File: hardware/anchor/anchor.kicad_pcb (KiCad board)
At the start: 2 copper layers, 50.1 x 50 mm, 94 parts, among them J2 USB_C_Receptacle_USB2.0_16P, J3 STM SWD, J4 BLE SWD, J5 BATTERY, SW1 SW_DIP_x03, SW2 RESET, SW3 BOOT, SW4 USER, U1 BQ24075RGT, U2 TPS63070RNMR, U3 USBLC6-2SC6, U4 STM32F411CEUx, U6 FSC-BT630, Y1 NX3225SA-24MHz

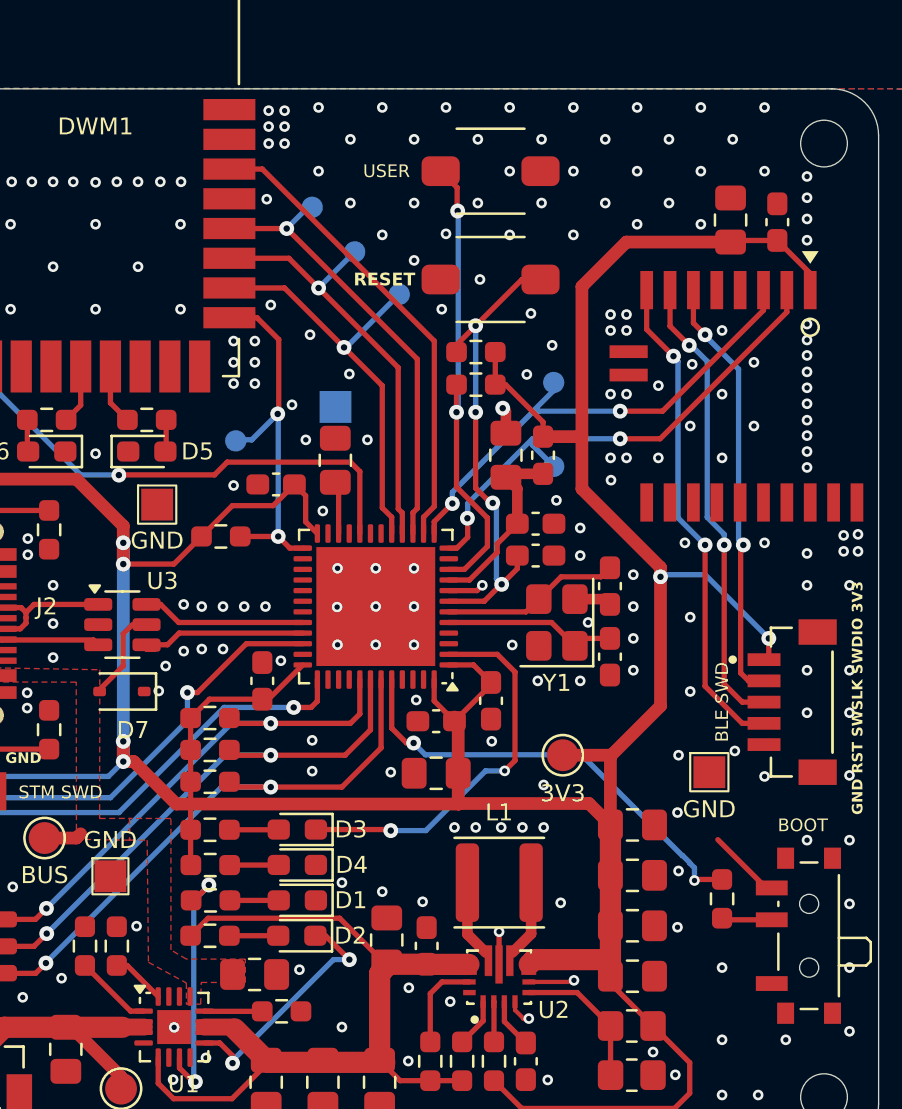
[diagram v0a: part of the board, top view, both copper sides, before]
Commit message: update(anchor): Clear DRC errors and release anchor rev 0.2
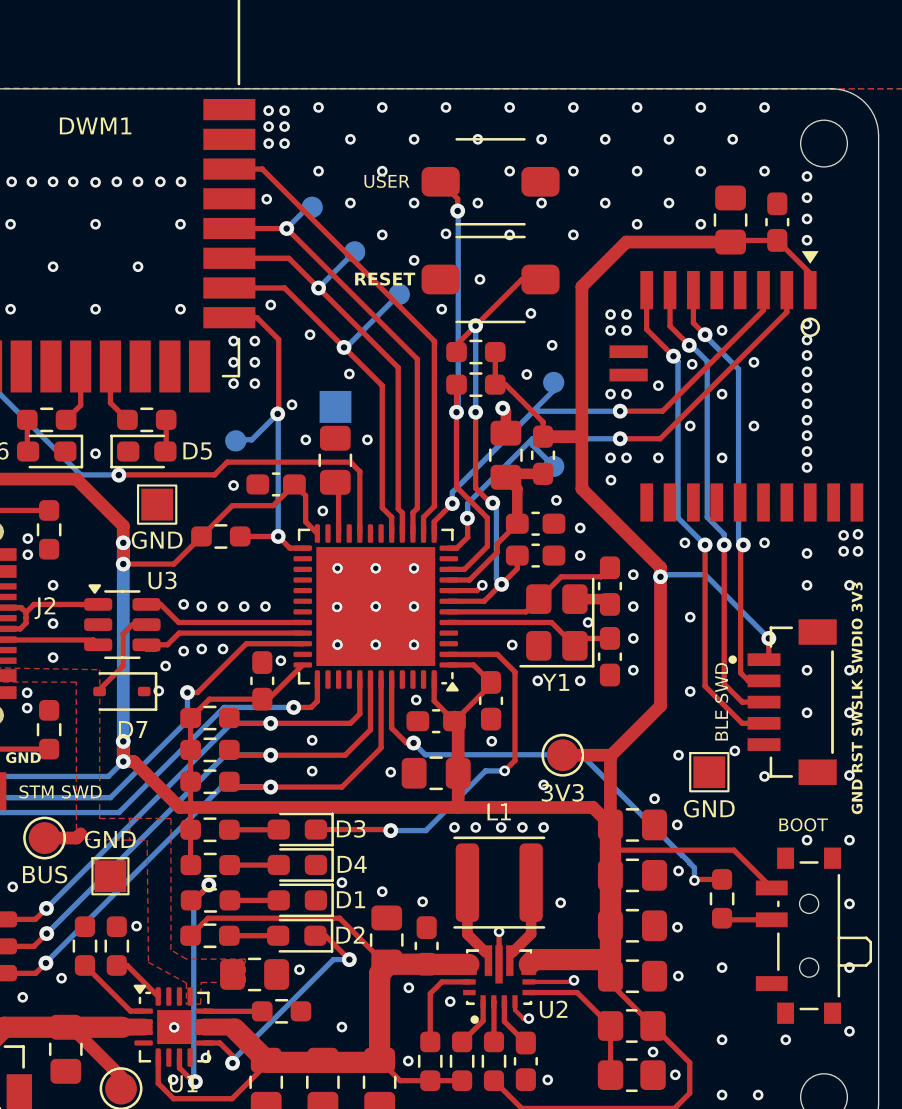
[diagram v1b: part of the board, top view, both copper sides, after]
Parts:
- moved SW4 0.50 mm to (224.1, 67.0)
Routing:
- net +3.3V: track 192.6 -> 197.8 mm
- net GND: vias 258 -> 261
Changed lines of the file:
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@@
 	(footprint "My_Tactile:SW_Tactile_SMD_3x4mm_2pin_update"
 		(layer "F.Cu")
-		(at 224.1 66.5 180)
+		(at 224.1 67 180)
 		(descr "Tactile switch SMD 2-pin, body 3x4x2 mm, pads 1.8x1.4 mm, 4.7 mm pitch")
 		(tags "tactile switch 3x4 2pin SMD")
@@
 	)
 	(via
+		(at 231.82 96.05)
+		(size 0.5)
+		(drill 0.25)
+		(layers "F.Cu" "B.Cu")
+		(free yes)
+		(net 1)
+	)
+	(via
 		(at 197.8 103)
 		(size 0.5)
@@
 	)
 	(via
-		(at 232.9 96.7)
+		(at 232.89 97.28)
 		(size 0.5)
 		(drill 0.25)
@@
 	)
 	(via
+		(at 219 66.5)
+		(size 0.5)
+		(drill 0.25)
+		(layers "F.Cu" "B.Cu")
+		(free yes)
+		(net 1)
+	)
+	(via
 		(at 233.5 91)
 		(size 0.5)
@@
 	)
 	(via
+		(at 232.94 104.4)
+		(size 0.5)
+		(drill 0.25)
+		(layers "F.Cu" "B.Cu")
+		(free yes)
+		(net 1)
+	)
+	(via
 		(at 223.5 65)
 		(size 0.5)
@@
 	)
 	(segment
+		(start 222.575 96.455)
+		(end 222.58 96.46)
+		(width 0.6)
+		(layer "F.Cu")
+		(net 5)
+	)
+	(segment
 		(start 210.8625 91.3625)
 		(end 213.35 91.3625)
@@
 	)
 	(segment
+		(start 209.975 96.46)
+		(end 209.975 96.325)
+		(width 0.25)
+		(layer "F.Cu")
+		(net 5)
+	)
+	(segment
 		(start 228.4 71.9296)
 		(end 230.4921 69.8375)
@@
 	)
 	(segment
+		(start 229.7425 97.283)
+		(end 228.9195 96.46)
+		(width 0.6)
+		(layer "F.Cu")
+		(net 5)
+	)
+	(segment
 		(start 209.975 92.25)
 		(end 209.975 91.94525)
@@
 	)
 	(segment
-		(start 222.625 96.275)
-		(end 222.6 96.3)
-		(width 0.6)
-		(layer "F.Cu")
-		(net 5)
-	)
-	(segment
-		(start 209.3 96.3)
-		(end 209.95 96.3)
-		(width 0.6)
-		(layer "F.Cu")
-		(net 5)
-	)
-	(segment
 		(start 199.4 81)
 		(end 198.7 81)
@@
 	)
 	(segment
+		(start 207.3 94.3)
+		(end 209.46 96.46)
+		(width 0.6)
+		(layer "F.Cu")
+		(net 5)
+	)
+	(segment
 		(start 229.7425 103.625)
 		(end 229.7425 104.40575)
@@
 	)
 	(segment
-		(start 209.975 96.275)
-		(end 209.95 96.3)
-		(width 0.25)
-		(layer "F.Cu")
-		(net 5)
-	)
-	(segment
 		(start 232.1 85.6)
 		(end 232.1 85.16)
@@
 	(segment
 		(start 229.7425 99.65725)
-		(end 229.7425 97.283)
+		(end 229.7425 98.41)
 		(width 1)
 		(layer "F.Cu")
@@
 	)
 	(segment
-		(start 222.575 96.275)
-		(end 222.6 96.3)
-		(width 0.6)
-		(layer "F.Cu")
-		(net 5)
-	)
-	(segment
 		(start 209.975 97.51)
 		(end 209.975 98.9875)
@@
 	)
 	(segment
-		(start 237.075 100.25)
-		(end 234.8 97.975)
-		(width 0.25)
+		(start 222.58 96.46)
+		(end 209.975 96.46)
+		(width 0.6)
 		(layer "F.Cu")
 		(net 5)
@@
 	)
 	(segment
-		(start 207.3 94.3)
-		(end 209.3 96.3)
+		(start 222.575 94.85)
+		(end 222.575 96.455)
 		(width 0.6)
 		(layer "F.Cu")
@@
 	)
 	(segment
-		(start 209.975 96.325)
-		(end 209.95 96.3)
+		(start 229.7425 98.41)
+		(end 229.8025 98.47)
 		(width 0.25)
 		(layer "F.Cu")
@@
 	)
 	(segment
+		(start 228.9195 96.46)
+		(end 222.58 96.46)
+		(width 0.6)
+		(layer "F.Cu")
+		(net 5)
+	)
+	(segment
 		(start 224.3 90.575)
 		(end 224.275 90.575)
@@
 	)
 	(segment
-		(start 228.7345 96.275)
-		(end 229.7425 97.283)
-		(width 0.6)
-		(layer "F.Cu")
-		(net 5)
-	)
-	(segment
 		(start 233.476 108.476)
 		(end 231.75 106.75)
@@
 	)
 	(segment
-		(start 222.6 96.3)
-		(end 209.95 96.3)
-		(width 0.6)
-		(layer "F.Cu")
-		(net 5)
-	)
-	(segment
 		(start 224.32125 76.55)
 		(end 224.32125 75.017005)
@@
 	(segment
 		(start 209.975 97.51)
-		(end 209.975 96.325)
+		(end 209.975 96.46)
 		(width 0.25)
 		(layer "F.Cu")
@@
 	)
 	(segment
-		(start 222.625 96.275)
-		(end 228.7345 96.275)
-		(width 0.6)
-		(layer "F.Cu")
-		(net 5)
-	)
-	(segment
 		(start 197.75 81)
 		(end 197.5 81)
@@
 	)
 	(segment
+		(start 229.8025 98.47)
+		(end 235.56 98.47)
+		(width 0.25)
+		(layer "F.Cu")
+		(net 5)
+	)
+	(segment
 		(start 222.575 92.575)
 		(end 222.4 92.4)
@@
 	)
 	(segment
+		(start 229.7425 98.41)
+		(end 229.7425 97.283)
+		(width 1)
+		(layer "F.Cu")
+		(net 5)
+	)
+	(segment
 		(start 206.80475 83.20475)
 		(end 204.6 81)
@@
 	)
 	(segment
+		(start 235.56 98.47)
+		(end 237.34 100.25)
+		(width 0.25)
+		(layer "F.Cu")
+		(net 5)
+	)
+	(segment
 		(start 237.6 69.7625)
 		(end 235.475 69.7625)
@@
 	)
 	(segment
-		(start 222.575 94.85)
-		(end 222.575 96.275)
+		(start 209.46 96.46)
+		(end 209.975 96.46)
 		(width 0.6)
 		(layer "F.Cu")
@@
 	)
 	(segment
-		(start 222.525 68.35)
-		(end 222.525 67.275)
+		(start 222.55 68.375)
+		(end 222.55 67.8)
 		(width 0.25)
 		(layer "F.Cu")
@@
 	)
 	(segment
-		(start 222.525 67.275)
-		(end 221.75 66.5)
-		(width 0.25)
-		(layer "F.Cu")
-		(net 31)
-	)
-	(segment
 		(start 222.49625 77.85)
 		(end 222.49625 76.55)
@@
 		(width 0.25)
 		(layer "F.Cu")
+		(net 31)
+	)
+	(segment
+		(start 222.55 67.8)
+		(end 221.75 67)
+		(width 0.25)
+		(layer "F.Cu")

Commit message: update(hw): Apply design changes to anchor
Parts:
- removed C3: 10u, Capacitor_SMD:C_0805_2012Metric_Pad1.18x1.45mm_HandSolder
- removed the D1 at (215.0, 100.8)
- removed the R14 at (224.3, 108.4)
- removed the R3 at (210.9, 99.2)
- removed the R5 at (206.5, 103.0)
- removed the SW3 at (238.8, 102.5)
- removed TP15: BATT, TestPoint:TestPoint_Pad_D1.5mm
- added C13: 22u, Capacitor_SMD:C_0805_2012Metric_Pad1.18x1.45mm_HandSolder, F.Cu at (235.4, 100.9)
- added C24: DNP, Capacitor_SMD:C_01005_0402Metric, F.Cu at (241.1, 85.5)
- added C26: DNP, Capacitor_SMD:C_01005_0402Metric, F.Cu at (241.1, 88.0)
- added D5: RED, LED_SMD:LED_0603_1608Metric_Pad1.05x0.95mm_HandSolder, F.Cu at (215.9, 100.3)
- added J3: BLE_Conn, Connector_Coaxial:U.FL_Hirose_U.FL-R-SMT-1_Vertical, F.Cu at (238.2, 88.8)
- added L2: DNP, Inductor_SMD:L_0402_1005Metric, F.Cu at (241.4, 86.8)
- added Q1: AO664, Package_SO:TSOP-6_1.65x3.05mm_P0.95mm, F.Cu at (219.3, 106.1)
- added R18: 10K, Resistor_SMD:R_0603_1608Metric_Pad0.98x0.95mm_HandSolder, F.Cu at (219.8, 94.6)
- added R22: 2.2k, Resistor_SMD:R_0603_1608Metric_Pad0.98x0.95mm_HandSolder, F.Cu at (212.0, 97.3)
- added R23: 2.2k, Resistor_SMD:R_0603_1608Metric_Pad0.98x0.95mm_HandSolder, F.Cu at (212.0, 100.3)
- added R6: 3.56k, Resistor_SMD:R_0603_1608Metric_Pad0.98x0.95mm_HandSolder, F.Cu at (212.0, 103.0)
- added R7: 10k, Resistor_SMD:R_0603_1608Metric_Pad0.98x0.95mm_HandSolder, F.Cu at (209.7, 103.9)
- added R8: 470k, Resistor_SMD:R_0805_2012Metric_Pad1.20x1.40mm_HandSolder, F.Cu at (235.4, 108.1)
- added SW1: PWR, Button_Switch_SMD:SW_Push_1P1T-MP_NO_Horizontal_Alps_SKRTLAE010, F.Cu at (217.6, 111.0)
- added TP11: BATT, TestPoint:TestPoint_Pad_D1.5mm, F.Cu at (205.7, 108.9)
- added TP16: SYS, TestPoint:TestPoint_Pad_D1.5mm, F.Cu at (220.2, 101.0)
- added U4: BQ24075RGT, Package_DFN_QFN:VQFN-16-1EP_3x3mm_P0.5mm_EP1.6x1.6mm, F.Cu at (213.9, 106.1)
- C10, C11: value 22u -> 10u
- C12: value DNP -> 22u
- C5: value 1u -> 100n; footprint Capacitor_SMD:C_0805_2012Metric_Pad1.18x1.45mm_HandSolder -> Capacitor_SMD:C_0603_1608Metric_Pad1.08x0.95mm_HandSolder
- C6: value 4.7u -> 100n; footprint Capacitor_SMD:C_0805_2012Metric_Pad1.18x1.45mm_HandSolder -> Capacitor_SMD:C_0603_1608Metric_Pad1.08x0.95mm_HandSolder
- C7: value 4.7u -> 1u
- C8: value 100n -> 1u
- C9: value 10u -> 4.7u
- D2: value YELLOW -> GREEN
- R10: value 6k -> 10k
- R11: value 6k -> 100k
- R12: value 470k -> 10k; footprint Resistor_SMD:R_0805_2012Metric_Pad1.20x1.40mm_HandSolder -> Resistor_SMD:R_0603_1608Metric_Pad0.98x0.95mm_HandSolder
- R13: value 150k -> 10k; footprint Resistor_SMD:R_0805_2012Metric_Pad1.20x1.40mm_HandSolder -> Resistor_SMD:R_0603_1608Metric_Pad0.98x0.95mm_HandSolder
- R19: value 10K -> 2.2k
- R2: value 3.1k -> 10k
- R4: value 10k -> 3.1k
- R9: value 10k -> 150k; footprint Resistor_SMD:R_0603_1608Metric_Pad0.98x0.95mm_HandSolder -> Resistor_SMD:R_0805_2012Metric_Pad1.20x1.40mm_HandSolder
- TP3: footprint TestPoint:TestPoint_Pad_D1.5mm -> TestPoint:TestPoint_Pad_D1.0mm
- U1: value BQ24075RGT -> MAX17048G_T10; footprint Package_DFN_QFN:VQFN-16-1EP_3x3mm_P0.5mm_EP1.6x1.6mm -> Package_SON:SON-8-1EP_3x2mm_P0.5mm_EP1.4x1.6mm
- U5: renamed from U6; footprint Other_Footprint:FSC-BT630 -> other_footprint:FSC-BT630
- moved R9 31.3 mm to (235.4, 110.4), turned to 0 degrees
- moved C6 28.5 mm to (232.5, 110.1)
- moved J5 27.3 mm to (232.8, 64.9), turned to 0 degrees
- moved D2 24.4 mm to (233.7, 86.9), turned to 90 degrees
- moved R10 21.5 mm to (230.9, 110.1), turned to -90 degrees
- moved C9 20.8 mm to (210.6, 109.2), turned to -90 degrees
- moved R2 14.1 mm to (227.7, 110.1), turned to -90 degrees
- moved R19 13.9 mm to (235.2, 86.9)
- moved R11 12.3 mm to (222.6, 104.7), turned to 90 degrees
- moved C11 11.5 mm to (219.3, 103.3)
- moved C2 9.42 mm to (225.6, 108.6)
- moved R13 8.89 mm to (221.9, 108.4), turned to 90 degrees
- moved R12 8.47 mm to (223.6, 102.2)
- moved R4 8.08 mm to (223.6, 100.7), turned to 0 degrees
- moved TP4 7.97 mm to (239.4, 101.0)
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- renumbered C23 to C15, C13 to C16, C22 to C17, C14 to C18, C15 to C19, C16 to C20, C17 to C21, C18 to C22, C19 to C23, C20 to C25, C21 to C27, C24 to C28, C25 to C29, C26 to C30, D7 to D1, D5 to D6, D6 to D7, J5 to J1, J3 to J4, J4 to J5, R15 to R14, R16 to R15, R17 to R16, R18 to R17, R22 to R24, R23 to R25, R24 to R26, R7 to R3, R8 to R5, SW1 to SW2, SW2 to SW3, TP9 to TP10, TP10 to TP12, TP11 to TP13, TP12 to TP14, TP13 to TP7, TP7 to TP8, TP8 to TP9, U4 to U6
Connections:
- C11 pad 1: +3.3V -> /SYS
- C5 pad 1: GND -> +BATT
- C5 pad 2: VBUS -> GND
- C6 pad 1: +BATT -> Net-(U2-VAUX)
- C7 pad 1: /SYS -> GND
- C7 pad 2: GND -> VBUS
- C8 pad 1: Net-(U2-VAUX) -> GND
- C8 pad 2: GND -> Net-(C8-Pad2)
- C9 pad 1: +3.3V -> +BATT
- D2 pad 1: /CHG -> GND
- D3 pad 1: /LED_USR -> GND
- D4 pad 1: GND -> /LED_USR
- R10 pad 1: /SYS -> Net-(U2-PG)
- R10 pad 2: Net-(D2-A) -> +3.3V
- R11 pad 1: Net-(D1-A) -> Net-(C8-Pad2)
- R11 pad 2: /PGOOD -> Net-(Q1B-G2)
- R12 pad 1: +3.3V -> Net-(Q1B-G2)
- R12 pad 2: /FB -> /SYS
- R13 pad 1: /FB -> Net-(Q1A-G1)
- R13 pad 2: GND -> /LOAD
- R19 pad 1: Net-(SW3-B) -> Net-(D2-A)
- R19 pad 2: Net-(U4-BOOT0) -> Net-(U5-P0.03)
- R2 pad 1: Net-(U1-ILIM) -> Net-(U2-EN)
- R2 pad 2: GND -> /SYS
- R21 pad 2: +3.3V -> /LED_PM
- R4 pad 1: Net-(U2-EN) -> Net-(U4-ILIM)
- R4 pad 2: /SYS -> GND
- R9 pad 1: GND -> /FB
- R9 pad 2: Net-(U1-TS) -> GND
- U1 pad 1: Net-(U1-TS) -> GND
- U1 pad 2: +BATT -> unconnected-(U1-CELL-Pad2)
- U1 pad 5: /SYS -> unconnected-(U1-~{ALERT}-Pad5)
- U1 pad 7: /PGOOD -> /PB8 / I2C1_SCL
- U1 pad 8: GND -> /PB9 / I2C1_SDA
- U1 pad 9: /CHG -> GND
- U5 pad 1: +3.3V -> /BLE_RX
- U5 pad 10: GND -> /BLE_SWDIO
- U5 pad 15: unconnected-(U6-P0.06-Pad15) -> Net-(U5-P0.03)
- U5 pad 19: unconnected-(U6-P0.10/NFC2-Pad19) -> GND
- U5 pad 20: unconnected-(U6-P0.11-Pad20) -> Net-(U5-EXT_ANT)
- U5 pad 3: /BLE_RX -> unconnected-(U5-I2C_SDA-Pad3)
- U5 pad 7: /BLE_SWDCLK -> +3.3V
- U5 pad 8: /BLE_SWDIO -> GND
- U5 pad 9: GND -> /BLE_SWDCLK
- U6 pad 38: unconnected-(U4-PA15-Pad38) -> /LED_PM
- U6 pad 44: Net-(U4-BOOT0) -> Net-(U6-BOOT0)
- U6 pad 45: unconnected-(U4-PB8-Pad45) -> /PB9 / I2C1_SDA
- U6 pad 46: unconnected-(U4-PB9-Pad46) -> /PB8 / I2C1_SCL
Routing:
- net +3.3V: track 197.8 -> 163.5 mm, vias 7 -> 5
- net /BLE_SWDIO: track 23.3 -> 0.13 mm, vias 2 -> 0
- net /BLE_SWDCLK: track 21.9 -> 0.00 mm, vias 2 -> 0
- net Net-(U4-BOOT0): track 21.2 -> 0.00 mm, vias 2 -> 0
- net /PB8 / I2C1_SCL: track 0.00 -> 21.0 mm, vias 0 -> 2
- net /PB9 / I2C1_SDA: track 0.00 -> 20.8 mm, vias 0 -> 2
- net /BLE_RST: track 20.3 -> 0.00 mm, vias 2 -> 0
- net /SYS: track 41.0 -> 22.1 mm
- net /LED_USR: track 18.4 -> 3.46 mm, vias 2 -> 0
- net Net-(C8-Pad2): track 0.00 -> 14.0 mm, vias 0 -> 2
- net /LED_PM: track 0.00 -> 13.9 mm, vias 0 -> 2
- net /PGOOD: track 12.3 -> 0.00 mm, vias 2 -> 0
- net /CHG: track 11.6 -> 0.00 mm, vias 2 -> 0
- net Net-(Q1A-G1): track 0.00 -> 11.2 mm, vias 0 -> 2
- net Net-(U4-ILIM): track 0.00 -> 8.85 mm, vias 0 -> 2
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- added copper zone on F.Cu, net /LOAD
- added copper zone on F.Cu, net /SYS
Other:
- board text removed: "UWB-RTLS"

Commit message: feat: Release final hardware for tag & anchor
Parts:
- removed C8: 1u, Capacitor_SMD:C_0603_1608Metric_Pad1.08x0.95mm_HandSolder
- removed Q1: AO664, Package_SO:TSOP-6_1.65x3.05mm_P0.95mm
- removed the TP3 at (216.8, 77.6)
- added C3: 100n, Capacitor_SMD:C_0603_1608Metric_Pad1.08x0.95mm_HandSolder, F.Cu at (224.2, 104.7)
- added J10: Conn_01x02, Connector_Wire:SolderWire-0.1sqmm_1x02_P3.6mm_D0.4mm_OD1mm, F.Cu at (198.6, 111.2)
- added J6: I2C, Other_Footprint:JST_BM04B-SRSS-TB_LF__SN_, F.Cu at (240.0, 95.3)
- added Q2: AO3404A, Package_TO_SOT_SMD:SOT-23, F.Cu at (219.8, 102.0)
- added Q3: AO3407A, Package_TO_SOT_SMD:SOT-23, F.Cu at (219.8, 106.1)
- added R27: 10k, Resistor_SMD:R_0603_1608Metric_Pad0.98x0.95mm_HandSolder, F.Cu at (227.4, 93.2)
- added R28: 10k, Resistor_SMD:R_0603_1608Metric_Pad0.98x0.95mm_HandSolder, F.Cu at (227.4, 94.7)
- C11: footprint Capacitor_SMD:C_0805_2012Metric_Pad1.18x1.45mm_HandSolder -> Capacitor_SMD:C_0805_2012Metric
- C24, C26: footprint Capacitor_SMD:C_01005_0402Metric -> Capacitor_SMD:C_0402_1005Metric
- D3: value YELLOW -> GREEN
- J4: value STM SWD -> BM06B-SRSS-TB_LF__SN_; footprint Other_Footprint:JST_BM04B-SRSS-TB_LF__SN_ -> Connector_JST:JST_SH_BM06B-SRSS-TB_1x06-1MP_P1.00mm_Vertical
- R11: value 100k -> 10k
- R12: value 10k -> 100k
- TP10: value TestPoint -> TX
- TP12: value TestPoint -> MISO
- TP13: value TestPoint -> CS1
- TP14: value TestPoint -> RX
- TP4: footprint TestPoint:TestPoint_Pad_D1.5mm -> TestPoint:TestPoint_Pad_1.0x1.0mm; moved to B.Cu
- TP8: value TestPoint -> SCK
- TP9: value TestPoint -> MOSI
- moved TP16 240.6 mm to (1.27, 1.27)
- moved TP4 27.7 mm to (226.9, 76.3), turned to 180 degrees
- moved D4 25.2 mm to (240.1, 104.4)
- moved D5 24.9 mm to (240.1, 106.1)
- moved D3 24.5 mm to (240.1, 102.7)
- moved R22 16.4 mm to (227.4, 91.8)
- moved D2 15.5 mm to (240.1, 101.0), turned to 180 degrees
- moved R21 14.0 mm to (225.7, 101.3), turned to -90 degrees
- moved TP8 11.6 mm to (220.7, 78.7)
- moved TP7 9.96 mm to (210.9, 99.4)
- moved R23 8.93 mm to (219.8, 96.0)
- moved R13 6.33 mm to (223.3, 102.3), turned to 180 degrees
- moved TP12 5.70 mm to (219.7, 75.7)
- moved TP9 5.35 mm to (219.0, 77.6)
- moved TP5 4.81 mm to (228.3, 97.2)
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- renumbered TP2 to TP3
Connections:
- C1 pad 1: /SYS -> /LOAD
- C2 pad 1: /SYS -> /LOAD
- C4 pad 1: /SYS -> /LOAD
- D4 pad 1: /LED_USR -> /CHG
- J4 pad 1: +3.3V -> /PA10 / UART1_RX
- J4 pad 2: /STM_SWDCLK -> /PA9 / UART1_TX
- J4 pad 3: /STM_SWDIO -> /STM_SWDCLK
- J4 pad 4: GND -> /STM_SWDIO
- J5 pad 1: +3.3V -> /BLE_SWDCLK
- J5 pad 2: /BLE_RST -> /BLE_SWDIO
- J5 pad 3: /BLE_SWDCLK -> /BLE_RST
- J5 pad 4: /BLE_SWDIO -> GND
- J5 pad 5: GND -> +3.3V
- R1 pad 2: /SYS -> /LOAD
- R11 pad 1: Net-(C8-Pad2) -> Net-(Q2-G)
- R11 pad 2: Net-(Q1B-G2) -> /LOAD
- R12 pad 1: Net-(Q1B-G2) -> Net-(C3-Pad2)
- R12 pad 2: /SYS -> Net-(Q2-D)
- R13 pad 1: Net-(Q1A-G1) -> Net-(Q2-D)
- R13 pad 2: /LOAD -> /SYS
- R2 pad 2: /SYS -> /LOAD
- R21 pad 1: Net-(D3-A) -> Net-(D4-A)
- R21 pad 2: /LED_PM -> /SYS
- R22 pad 1: Net-(D4-A) -> Net-(D3-A)
- R22 pad 2: +3.3V -> /LED_USR
- SW1 pad 1: Net-(C8-Pad2) -> Net-(C3-Pad2)
- SW1 pad 2: Net-(Q1A-G1) -> Net-(Q2-G)
- U2 pad 12_13: /SYS -> /LOAD
- U4 pad 4: GND -> /CHARGE_EN
- U4 pad 9: unconnected-(U4-~{CHG}-Pad9) -> /CHG
- U6 pad 30: unconnected-(U6-PA9-Pad30) -> /PA9 / UART1_TX
- U6 pad 31: unconnected-(U6-PA10-Pad31) -> /PA10 / UART1_RX
- U6 pad 38: /LED_PM -> /CHARGE_EN
- U6 pad 45: /PB9 / I2C1_SDA -> /PB8 / I2C1_SCL
- U6 pad 46: /PB8 / I2C1_SCL -> /PB9 / I2C1_SDA
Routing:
- net /PA9 / UART1_TX: track 0.00 -> 31.1 mm, vias 0 -> 2
- net /PA10 / UART1_RX: track 0.00 -> 31.0 mm, vias 0 -> 2
- net /CHG: track 0.00 -> 30.0 mm, vias 0 -> 2
- net /PB9 / I2C1_SDA: track 20.8 -> 43.7 mm, vias 2 -> 6
- net +3.3V: track 163.5 -> 185.9 mm
- net /PB8 / I2C1_SCL: track 21.0 -> 43.1 mm, vias 2 -> 6
- net Net-(D5-A): track 2.13 -> 24.2 mm, vias 0 -> 2
- net /CHARGE_EN: track 0.00 -> 19.7 mm, vias 0 -> 2
- net /BLE_SWDIO: track 0.13 -> 17.0 mm, vias 0 -> 2
- net Net-(D4-A): track 2.13 -> 18.2 mm, vias 0 -> 2
- net Net-(Q2-G): track 0.00 -> 15.5 mm, vias 0 -> 2
- net /BLE_SWDCLK: track 0.00 -> 15.1 mm, vias 0 -> 2
- net Net-(D3-A): track 2.13 -> 16.7 mm, vias 0 -> 2
- net Net-(C8-Pad2): track 14.0 -> 0.00 mm, vias 2 -> 0
- net /LED_PM: track 13.9 -> 0.00 mm, vias 2 -> 0
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- added copper zone on F.Cu, net +BATT
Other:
- outline, holes or cut-outs redrawn
- board text added: "ANCHOR|REV: v1.0"
- board text added: "CLK DIO RST GND 3V3"
- board text added: "PRODUCTION BOARD REL: 2025-04-13"
- board text added: "RX TX CLK DIO 3V3 GND"
- board text added: "SDA SCL GND 3V3"
- board text added: "UWB-RTLS"
- board text removed: "3V3 SWSLK SWDIO GND"
- board text removed: "BOARD: ANCHOR REV v0.2"
- board text removed: "GND RST SWSLK SWDIO 3V3"

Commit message: feat: release final final hardware for tag + anchor
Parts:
- added D9: MBR230LSFT1G, Diode_SMD:D_SOD-123, F.Cu at (220.6, 107.3)
- added R29: 1k(TBD), Resistor_SMD:R_0603_1608Metric, F.Cu at (221.5, 109.3)
- added R30: 10k, Resistor_SMD:R_0603_1608Metric, F.Cu at (212.0, 110.0)
- C1, C10, C12, C13, C2, C7, C9: footprint Capacitor_SMD:C_0805_2012Metric_Pad1.18x1.45mm_HandSolder -> Capacitor_SMD:C_0805_2012Metric
- C3: value 100n -> 100n(TBD); footprint Capacitor_SMD:C_0603_1608Metric_Pad1.08x0.95mm_HandSolder -> Capacitor_SMD:C_0603_1608Metric
- C4, C5, C6: footprint Capacitor_SMD:C_0603_1608Metric_Pad1.08x0.95mm_HandSolder -> Capacitor_SMD:C_0603_1608Metric
- R1, R10, R11, R12, R13, R2, R21, R4, R6, R7: footprint Resistor_SMD:R_0603_1608Metric_Pad0.98x0.95mm_HandSolder -> Resistor_SMD:R_0603_1608Metric
- moved TP16 237.4 mm to (217.4, 99.3)
- moved R4 13.8 mm to (213.4, 110.0), turned to -90 degrees
- moved R21 5.73 mm to (220.2, 99.8), turned to 180 degrees
- moved C3 4.94 mm to (223.6, 99.8), turned to 180 degrees
- moved Q2 4.33 mm to (223.6, 104.1)
- moved R12 3.63 mm to (223.6, 101.2), turned to 180 degrees
- moved R13 3.29 mm to (220.2, 101.3)
- moved TP7 2.72 mm to (213.6, 99.2)
- moved Q3 1.95 mm to (220.2, 104.1)
- moved R11 1.65 mm to (221.5, 110.7), turned to 180 degrees
- moved C9 0.50 mm to (210.2, 109.2)
- moved R2 0.42 mm to (227.8, 110.1)
- moved C1 0.41 mm to (224.0, 108.5)
- moved C2 0.41 mm to (225.9, 108.5)
- moved C4 0.38 mm to (226.1, 104.7)
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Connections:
- Q3 pad 3: /LOAD -> Net-(D9-A)
- R11 pad 2: /LOAD -> Net-(D9-A)
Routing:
- net Net-(C3-Pad2): track 9.34 -> 20.0 mm
- net /SYS: track 17.2 -> 12.5 mm, vias 2 -> 0
- net Net-(D9-A): track 0.00 -> 3.59 mm
- net Net-(D4-A): track 18.2 -> 21.6 mm
- net Net-(Q2-G): track 15.5 -> 18.8 mm, vias 2 -> 4
- net /CHARGE_EN: track 19.7 -> 21.6 mm
- net Net-(U4-ILIM): track 9.16 -> 7.72 mm
- net GND: track 14.2 -> 13.3 mm, vias 304 -> 285
- added copper zone on F.Cu, net Net-(D9-A)
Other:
- board text added: "ANCHOR|REV: v1.1"
- board text added: "PRODUCTION BOARD REL: 2025-05-06"
- board text removed: "ANCHOR|REV: v1.0"
- board text removed: "PRODUCTION BOARD REL: 2025-04-13"

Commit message: Update: schematic with new dimensions and additional notes
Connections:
- Q2 pad 1: Net-(Q2-G) -> /PWR_LATCH
- R11 pad 1: Net-(Q2-G) -> /PWR_LATCH
- SW1 pad 2: Net-(Q2-G) -> /PWR_LATCH
- U6 pad 39: unconnected-(U6-PB3-Pad39) -> /PWR_LATCH
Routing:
- net /PWR_LATCH: track 0.00 -> 34.3 mm, vias 0 -> 5
- net Net-(Q2-G): track 18.8 -> 0.00 mm, vias 4 -> 0
- net GND: vias 285 -> 290
